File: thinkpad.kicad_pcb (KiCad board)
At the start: 2 copper layers, 287 x 120.5 mm, 125 parts, among them J1 Conn_01x06_MountingPin, J2 Conn_01x20_Socket, J3 Conn_01x06_Socket, SW1 SW_Push, U1 Raspberry_Pi_Pico

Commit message: Fix gnd
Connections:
- J1 pad MP: unconnected-(J1-MountPin-PadMP) -> GND
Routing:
- net unconnected-(J1-MountPin-PadMP): track 5.70 -> 0.00 mm
- added copper zone on B.Cu, net GND
- added copper zone on F.Cu, net GND
- removed copper zone on B.Cu, net (none)
- removed copper zone on F.Cu, net (none)

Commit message: Improvements
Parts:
- added JP1: SolderJumper_3_Open, Jumper:SolderJumper-3_P1.3mm_Open_Pad1.0x1.5mm_NumberLabels, F.Cu at (225.5, 156.7)
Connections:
- U1 pad 13: Col 2 -> unconnected-(U1-GND-Pad13)
- U1 pad 14: Col 1 -> Col 2
- U1 pad 15: Col 0 -> Col 1
- U1 pad 16: unconnected-(U1-GPIO12-Pad16) -> Col 0
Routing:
- net VCC: track 67.7 -> 77.4 mm, vias 1 -> 3
- net SC_DTCT: track 0.00 -> 6.45 mm

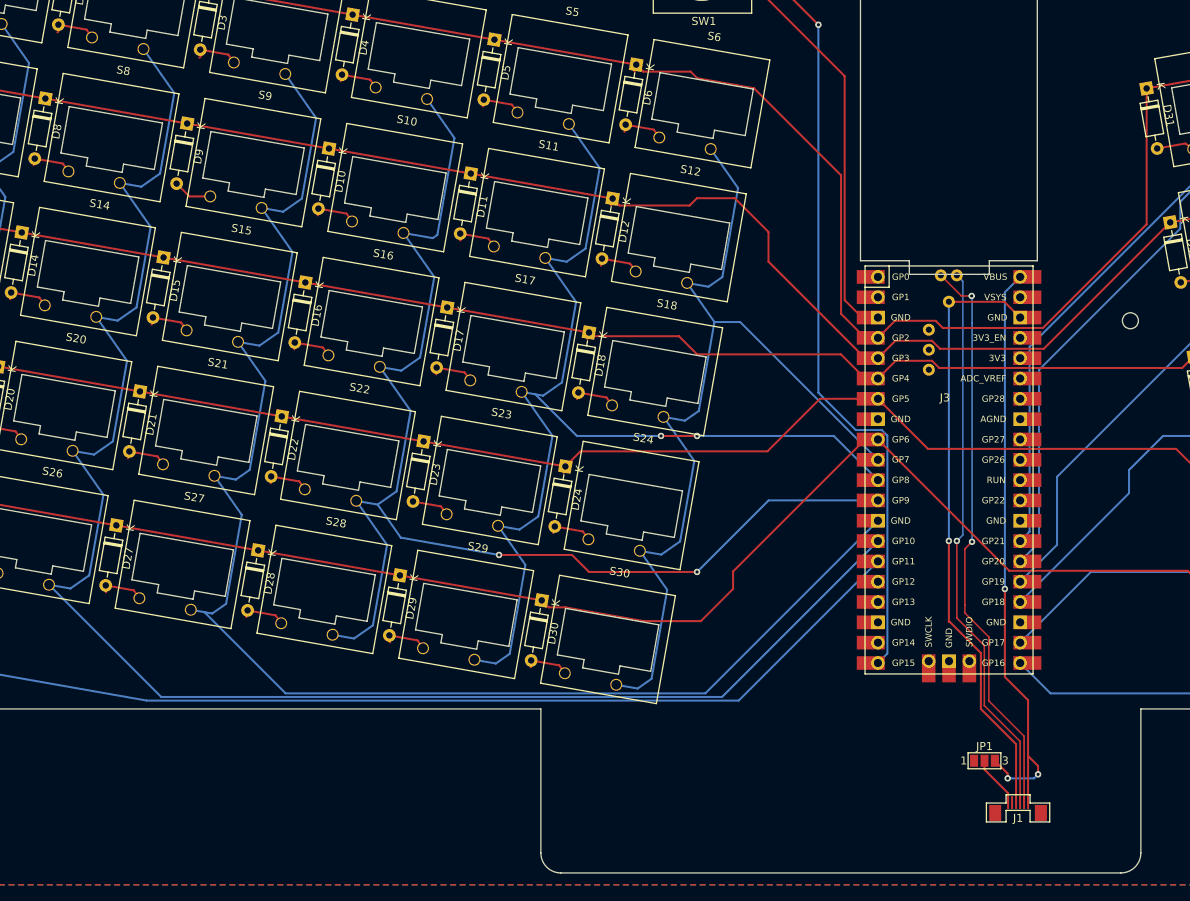
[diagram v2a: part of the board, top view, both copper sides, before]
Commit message: Made space for touchpad, fixed connection of cols, added pads for touchpad i2c
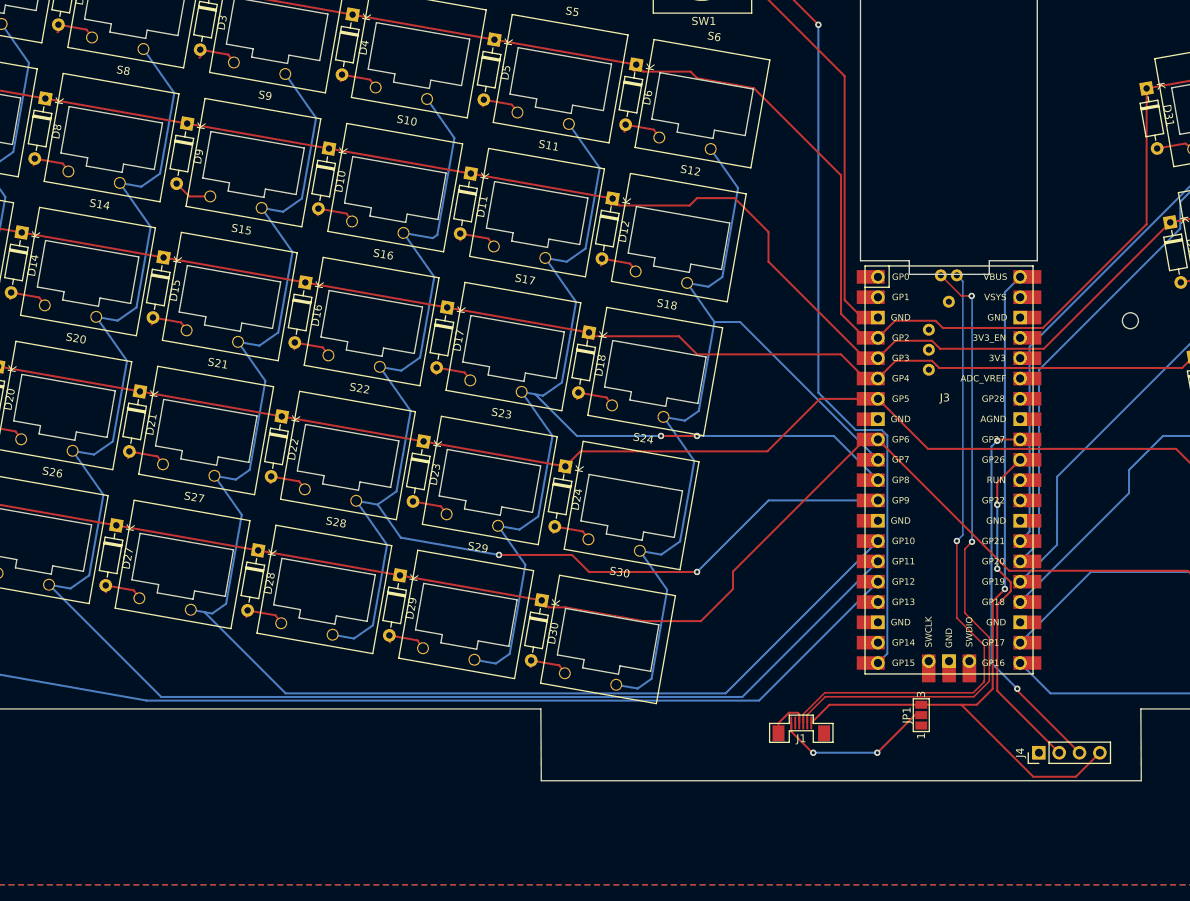
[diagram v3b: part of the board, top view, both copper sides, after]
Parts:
- added J4: Conn_01x04_Pin, Connector_PinHeader_2.54mm:PinHeader_1x04_P2.54mm_Vertical, F.Cu at (232.3, 155.7)
- moved J1 28.9 mm to (202.6, 151.9)
- moved JP1 9.74 mm to (217.6, 151.0), turned to 90 degrees
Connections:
- U1 pad 13: unconnected-(U1-GND-Pad13) -> GND
- U1 pad 18: unconnected-(U1-GND-Pad18) -> GND
- U1 pad 23: unconnected-(U1-GND-Pad23) -> GND
- U1 pad 28: unconnected-(U1-GND-Pad28) -> GND
- U1 pad 31: unconnected-(U1-GPIO26_ADC0-Pad31) -> SDA
- U1 pad 32: unconnected-(U1-GPIO27_ADC1-Pad32) -> SCL
- U1 pad 8: unconnected-(U1-GND-Pad8) -> GND
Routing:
- net GND: track 75.9 -> 5.57 mm, vias 1 -> 0
- net SCL: track 0.00 -> 46.8 mm, vias 0 -> 2
- net SDA: track 0.00 -> 42.4 mm, vias 0 -> 2
- net VCC: track 77.4 -> 99.7 mm, vias 3 -> 1
- net SC_DTCT: track 6.45 -> 20.4 mm, vias 0 -> 2
- net USB-: track 71.7 -> 80.2 mm
- net USB+: track 69.8 -> 78.2 mm
- net Col 0: track 222.8 -> 221.7 mm
- net Col 2: track 186.6 -> 185.5 mm
- net Col 1: track 207.6 -> 206.6 mm
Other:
- board size 287 x 120.5 mm -> 287 x 109 mm
